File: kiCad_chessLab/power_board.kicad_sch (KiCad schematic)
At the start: 0 parts

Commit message: Main Board update
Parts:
- added C69: 10uF, Capacitor_SMD:C_0603_1608Metric_Pad1.08x0.95mm_HandSolder, symbol Device:C
- added IC66: TP4056, chessLab-footprints:SOIC127P600X175-9N, symbol chessLab-symbols:TP4056
- added J4: DATA, CONN4_1048_KEY, symbol chessLab-symbols:1048
- added J5: PWR, CONN4_1048_KEY, symbol chessLab-symbols:1048
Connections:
- new net +3V3: J5.3
- new net +5V: J5.2
- new net BTN_PWR: J4.2
- new net GND: C69.1, IC66.6 (~{STDBY}), J4.4, J5.4
- new net PWR_HOLD: J4.1
- new net VBAT: C69.2, IC66.4 (VCC), J4.3
- new net VBUS: J5.1

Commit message: Complete Schematics
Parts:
- added C1, C5: 100uF, Capacitor_SMD:C_1206_3216Metric_Pad1.33x1.80mm_HandSolder, symbol Device:C
- added C3: 0.1uF, Capacitor_SMD:C_0603_1608Metric_Pad1.08x0.95mm_HandSolder, symbol Device:C
- added C4, C6, C7: 10uF, Capacitor_SMD:C_0603_1608Metric_Pad1.08x0.95mm_HandSolder, symbol Device:C
- added D1, D2: CHARGE, LED_SMD:LED_0603_1608Metric_Pad1.05x0.95mm_HandSolder, symbol Device:LED
- added D3: SS34, Diode_SMD:D_SMA, symbol Diode:SS34
- added IC1: MT3608, SOT95P280X145-6N, symbol chessLab-symbols:MT3608
- added IC3: DW01A-G, chessLab-footprints:SOT95P280X135-6N, symbol chessLab-symbols:DW01A-G
- added J3: AUX, CONN4_1048_KEY, symbol chessLab-symbols:1048
- added L1: CDRH4D28NP-2R2NC, chessLab-footprints:CDRH4D28NP100NC, symbol chessLab-symbols:CDRH4D28NP-2R2NC
- added Q1: FS8205A, chessLab-footprints:SOP65P640X120-8N, symbol chessLab-symbols:FS8205A
- added Q2: AO3401A, Package_TO_SOT_SMD:SOT-23_Handsoldering, symbol Transistor_FET:AO3401A
- added R1, R2, R7: 1k, Resistor_SMD:R_0603_1608Metric_Pad0.98x0.95mm_HandSolder, symbol Device:R
- added R3: 100, Resistor_SMD:R_0603_1608Metric_Pad0.98x0.95mm_HandSolder, symbol Device:R
- added R4: 220k, Resistor_SMD:R_0603_1608Metric_Pad0.98x0.95mm_HandSolder, symbol Device:R
- added R5: 33k, Resistor_SMD:R_0603_1608Metric_Pad0.98x0.95mm_HandSolder, symbol Device:R
- added R6: 1.1k, Resistor_SMD:R_0603_1608Metric_Pad0.98x0.95mm_HandSolder, symbol Device:R
- added R8: 10k, Resistor_SMD:R_0603_1608Metric_Pad0.98x0.95mm_HandSolder, symbol Device:R
- added R9: 100k, Resistor_SMD:R_0603_1608Metric_Pad0.98x0.95mm_HandSolder, symbol Device:R
- added SW1: SW_SPST, symbol Switch:SW_SPST
- added TP1: VBUS, TestPoint:TestPoint_Plated_Hole_D2.0mm, symbol Connector:TestPoint
- added TP10: 3V3, TestPoint:TestPoint_Plated_Hole_D2.0mm, symbol Connector:TestPoint
- added TP13, TP3: GND, TestPoint:TestPoint_Plated_Hole_D2.0mm, symbol Connector:TestPoint
- added TP2: +BAT, TestPoint:TestPoint_Plated_Hole_D2.0mm, symbol Connector:TestPoint
- added TP4: 5V, TestPoint:TestPoint_Plated_Hole_D2.0mm, symbol Connector:TestPoint
- added TP5: VBAT, TestPoint:TestPoint_Plated_Hole_D2.0mm, symbol Connector:TestPoint
- added TP6: -BAT, TestPoint:TestPoint_Plated_Hole_D2.0mm, symbol Connector:TestPoint
- added TP7: PWR_HOLD, TestPoint:TestPoint_Plated_Hole_D2.0mm, symbol Connector:TestPoint
- added TP8: VSYS, TestPoint:TestPoint_Plated_Hole_D2.0mm, symbol Connector:TestPoint
- added TP9: BTN_PWR, TestPoint:TestPoint_Plated_Hole_D2.0mm, symbol Connector:TestPoint
- added U1: BAT, chessLab-footprints:x218650smd, symbol chessLab-symbols:1048
- added U2: AMS1117-3.3, Package_TO_SOT_SMD:SOT-223-3_TabPin2, symbol Regulator_Linear:AMS1117-3.3
- renumbered C69 to C2, IC66 to IC2, J4 to J1, J5 to J2
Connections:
- net BTN_PWR is gone; now on net GND: J1.2
- net +3V3: now also C7.1, J3.3, TP10.1, U2.2 (VO)
- net +5V: now also C5.1, D3.1 (K), J3.2, R4.1, TP4.1
- net GND: now also IC2.1 (TEMP), IC2.3 (GND), IC2.9 (EP), C1.2, C4.2, C5.2, C6.2, C7.2, IC1.2 (GND), J3.4, Q1.6 (S2_1), Q1.7 (S2_2), Q2.1 (G), R5.2, R6.2, R7.2, R8.1, R9.1, SW1.1 (A), SW1.2 (B), TP13.1, TP3.1, TP6.1, TP9.1, U2.1 (GND); no longer IC2.6 (~{STDBY})
- net PWR_HOLD: now also R8.2, TP7.1
- net VBAT: now also IC2.5 (BAT), C4.1, Q2.2 (S), R9.2, TP2.1, TP5.1, U1.4 (+_2); no longer C2.2, IC2.4 (VCC)
- net VBUS: now also C2.2, IC2.4 (VCC), IC2.8 (CE), D1.2 (A), D2.2 (A), TP1.1
- net at IC2.2 (PROG): now also R6.1
- net at IC2.7 (~{CHRG}): now also R1.2
- new net: D1.1 (K), R2.1
- new net: IC2.6 (~{STDBY}), R2.2
- new net: IC1.3 (FB), R4.2, R5.1
- new net: C3.2, IC3.6 (GND), Q1.2 (S1_1), Q1.3 (S1_2), U1.1 (-_1), U1.3 (-_2)
- new net: R3.1, U1.2 (+_1)
- new net: IC3.1 (OD), Q1.4 (G1)
- new net: IC3.2 (CS), R7.1
- new net: IC3.3 (OC), Q1.5 (G2)
- new net: C3.1, IC3.5 (VCC), R3.2
- new net: D2.1 (K), R1.1
- new net: Q1.1 (D12_1), Q1.8 (D12_2)
- new net: D3.2 (A), IC1.1 (SW), L1.2
- new net VSYS: C1.1, C6.1, IC1.4 (EN), IC1.5 (VIN), L1.1, Q2.3 (D), TP8.1, U2.3 (VI)
- no-connect marks 0 -> 2
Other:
- note added: "BATTERY PROTECTION"
- note added: "BOOST VBAT -> 5V"
- note added: "BTN ON/OFF SYSTEM"
- note added: "CONNECTORS"
- note added: "IC CHARGE"
- note added: "LDO 3.3V"
- note added: "ON/OFF SYSTEM"
- moved on the sheet: C2, IC2, J1, J2

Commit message: PCB SetUp
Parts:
- J1, J2, J3: footprint CONN4_1048_KEY -> Connector_JST:JST_XH_B4B-XH-A_1x04_P2.50mm_Vertical
- SW1: footprint (none) -> chessLab-footprints:B3U-1000P
- U1: footprint chessLab-footprints:x218650smd -> chessLab-footprints:CONN4_1048_KEY
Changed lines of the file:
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@@
 			)
 		)
-		(property "Footprint" "chessLab-footprints:x218650smd"
+		(property "Footprint" "chessLab-footprints:CONN4_1048_KEY"
 			(at 21.59 0.33 0)
 			(effects
@@
 		(pin "2"
 		)
+		(pin "5"
+		)
+		(pin "6"
+		)
 		(instances
 			(project ""
@@
 			)
 		)
-		(property "Footprint" ""
+		(property "Footprint" "chessLab-footprints:B3U-1000P"
 			(at 161.29 105.41 0)
 			(effects
@@
 			)
 		)
-		(property "Footprint" "CONN4_1048_KEY"
+		(property "Footprint" "Connector_JST:JST_XH_B4B-XH-A_1x04_P2.50mm_Vertical"
 			(at 220.98 26.67 0)
 			(effects
@@
 			)
 		)
-		(property "Footprint" "CONN4_1048_KEY"
+		(property "Footprint" "Connector_JST:JST_XH_B4B-XH-A_1x04_P2.50mm_Vertical"
 			(at 220.98 44.45 0)
 			(effects
@@
 			)
 		)
-		(property "Footprint" "CONN4_1048_KEY"
+		(property "Footprint" "Connector_JST:JST_XH_B4B-XH-A_1x04_P2.50mm_Vertical"
 			(at 220.98 62.23 0)
 			(effects

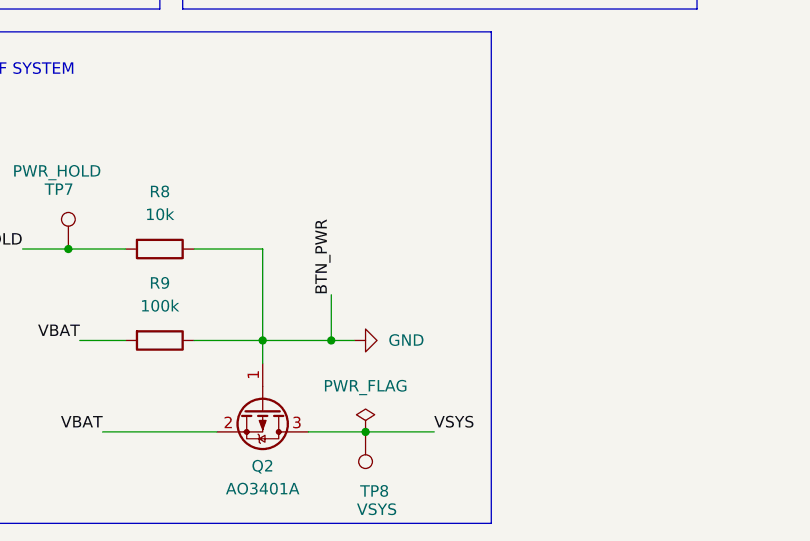
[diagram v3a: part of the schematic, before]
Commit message: Hall effect Replaced and 3d files uploaded
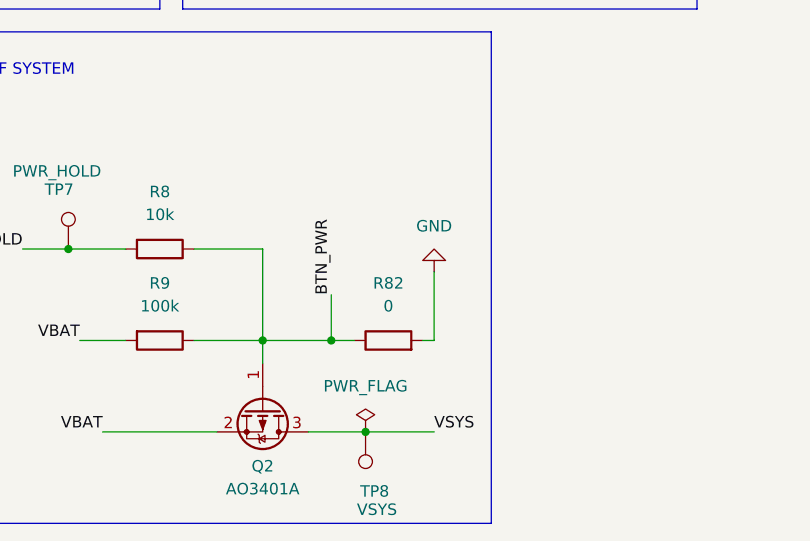
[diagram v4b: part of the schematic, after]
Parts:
- added R82: 0, Resistor_SMD:R_0603_1608Metric_Pad0.98x0.95mm_HandSolder, symbol Device:R
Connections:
- net GND: now also R82.2; no longer J1.2, Q2.1 (G), R8.1, R9.1, SW1.2 (B), TP9.1
- new net BTN_PWR: J1.2, Q2.1 (G), R8.1, R82.1, R9.1, SW1.2 (B), TP9.1
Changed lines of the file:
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@@
 	)
 	(junction
+		(at 156.21 175.26)
+		(diameter 0)
+		(color 0 0 0 0)
+	)
+	(junction
 		(at 83.82 191.77)
 		(diameter 0)
@@
 	)
 	(junction
-		(at 156.21 175.26)
-		(diameter 0)
-		(color 0 0 0 0)
-	)
-	(junction
 		(at 123.19 95.25)
 		(diameter 0)
@@
 	(wire
 		(pts
+			(xy 166.37 175.26) (xy 167.64 175.26)
+		)
+		(stroke
+			(width 0)
+			(type default)
+		)
+	)
+	(wire
+		(pts
 			(xy 36.83 39.37) (xy 36.83 44.45)
 		)
@@
 	(wire
 		(pts
+			(xy 167.64 175.26) (xy 167.64 167.64)
+		)
+		(stroke
+			(width 0)
+			(type default)
+		)
+	)
+	(wire
+		(pts
 			(xy 52.07 29.21) (xy 52.07 36.83)
 		)
@@
 	(wire
 		(pts
-			(xy 156.21 175.26) (xy 158.75 175.26)
-		)
-		(stroke
-			(width 0)
-			(type default)
-		)
-	)
-	(wire
-		(pts
 			(xy 127 165.1) (xy 133.35 165.1)
 		)
@@
 	(wire
 		(pts
+			(xy 156.21 175.26) (xy 158.75 175.26)
+		)
+		(stroke
+			(width 0)
+			(type default)
+		)
+	)
+	(wire
+		(pts
 			(xy 40.64 167.64) (xy 44.45 167.64)
 		)
@@
 	(symbol
 		(lib_id "Device:R")
+		(at 162.56 175.26 90)
+		(unit 1)
+		(exclude_from_sim no)
+		(in_bom yes)
+		(on_board yes)
+		(dnp no)
+		(fields_autoplaced yes)
+		(property "Reference" "R82"
+			(at 162.56 168.91 90)
+			(effects
+				(font
+					(size 1.27 1.27)
+				)
+			)
+		)
+		(property "Value" "0"
+			(at 162.56 171.45 90)
+			(effects
+				(font
+					(size 1.27 1.27)
+				)
+			)
+		)
+		(property "Footprint" "Resistor_SMD:R_0603_1608Metric_Pad0.98x0.95mm_HandSolder"
+			(at 162.56 177.038 90)
+			(effects
+				(font
+					(size 1.27 1.27)
+				)
+				(hide yes)
+			)
+		)
+		(property "Datasheet" "~"
+			(at 162.56 175.26 0)
+			(effects
+				(font
+					(size 1.27 1.27)
+				)
+				(hide yes)
+			)
+		)
+		(property "Description" "Resistor"
+			(at 162.56 175.26 0)
+			(effects
+				(font
+					(size 1.27 1.27)
+				)
+				(hide yes)
+			)
+		)
+		(pin "2"
+		)
+		(pin "1"
+		)
+		(instances
+			(project ""
+				(path "/767acb05-88fd-4294-8dd3-73f8ac75b0d1/337a5d50-bd96-4e85-84af-32e04ba9fe78"
+					(reference "R82")
+					(unit 1)
+				)
+			)
+		)
+	)
+	(symbol
+		(lib_id "Device:R")
 		(at 36.83 48.26 0)
 		(unit 1)
@@
 	(symbol
 		(lib_id "power:GND")
-		(at 158.75 175.26 90)
+		(at 167.64 167.64 180)
 		(unit 1)
 		(exclude_from_sim no)
@@
 		(fields_autoplaced yes)
 		(property "Reference" "#PWR012"
-			(at 165.1 175.26 0)
+			(at 167.64 161.29 0)
 			(effects
 				(font
@@
 		)
 		(property "Value" "GND"
-			(at 162.56 175.2599 90)
+			(at 167.64 162.56 0)
 			(effects
 				(font
 					(size 1.27 1.27)
 				)
-				(justify right)
 			)
 		)
 		(property "Footprint" ""
-			(at 158.75 175.26 0)
+			(at 167.64 167.64 0)
 			(effects
 				(font
@@
 		)
 		(property "Datasheet" ""
-			(at 158.75 175.26 0)
+			(at 167.64 167.64 0)
 			(effects
 				(font
@@
 		)
 		(property "Description" "Power symbol creates a global label with name \"GND\" , ground"
-			(at 158.75 175.26 0)
+			(at 167.64 167.64 0)
 			(effects
 				(font
